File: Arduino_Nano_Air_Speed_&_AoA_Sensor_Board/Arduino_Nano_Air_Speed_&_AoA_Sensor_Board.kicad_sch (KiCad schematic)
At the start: 7 parts, among them IC1 MPXV7007DP, J1 Conn_01x04, J2 Conn_01x02_Socket, J3 Conn_01x07_Pin, J4 Conn_01x02_Pin, J5 Conn_01x02_Pin

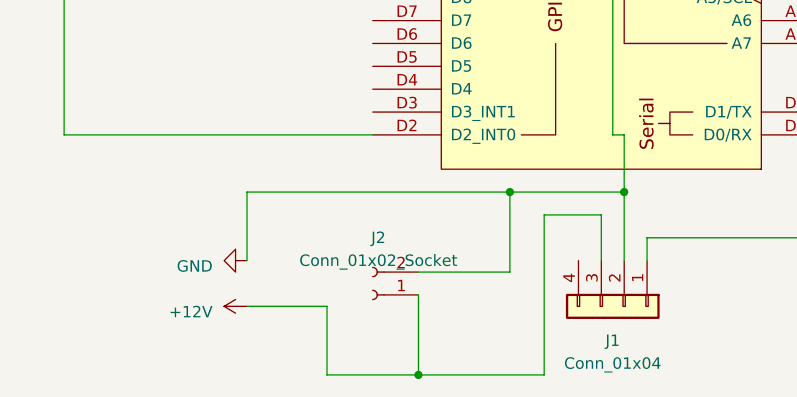
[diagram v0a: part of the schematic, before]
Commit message: Created a new board for the Wit-Motion WT901B IMU chip.
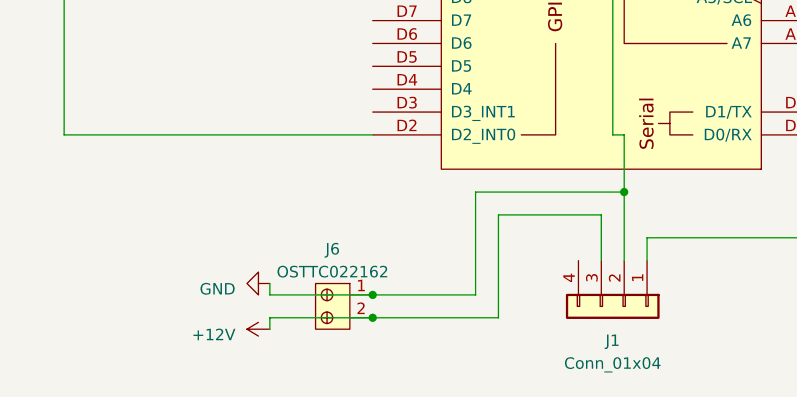
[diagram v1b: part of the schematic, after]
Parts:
- removed J2: Conn_01x02_Socket, Connector_PinSocket_2.54mm:PinSocket_1x02_P2.54mm_Vertical, symbol Connector:Conn_01x02_Socket
- added J6: OSTTC022162, digikey-footprints:Term_Block_1x2_P5.08MM, symbol dk_Terminal-Blocks-Wire-to-Board:OSTTC022162
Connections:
- net +12V: now also J6.2
- net GND: now also J6.1
